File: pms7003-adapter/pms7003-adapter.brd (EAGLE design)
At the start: 36.7 x 19.8 mm, 8 parts, among them J1 LPPB052CFFN-RC, U1 ATECC508A-SSHDA-T

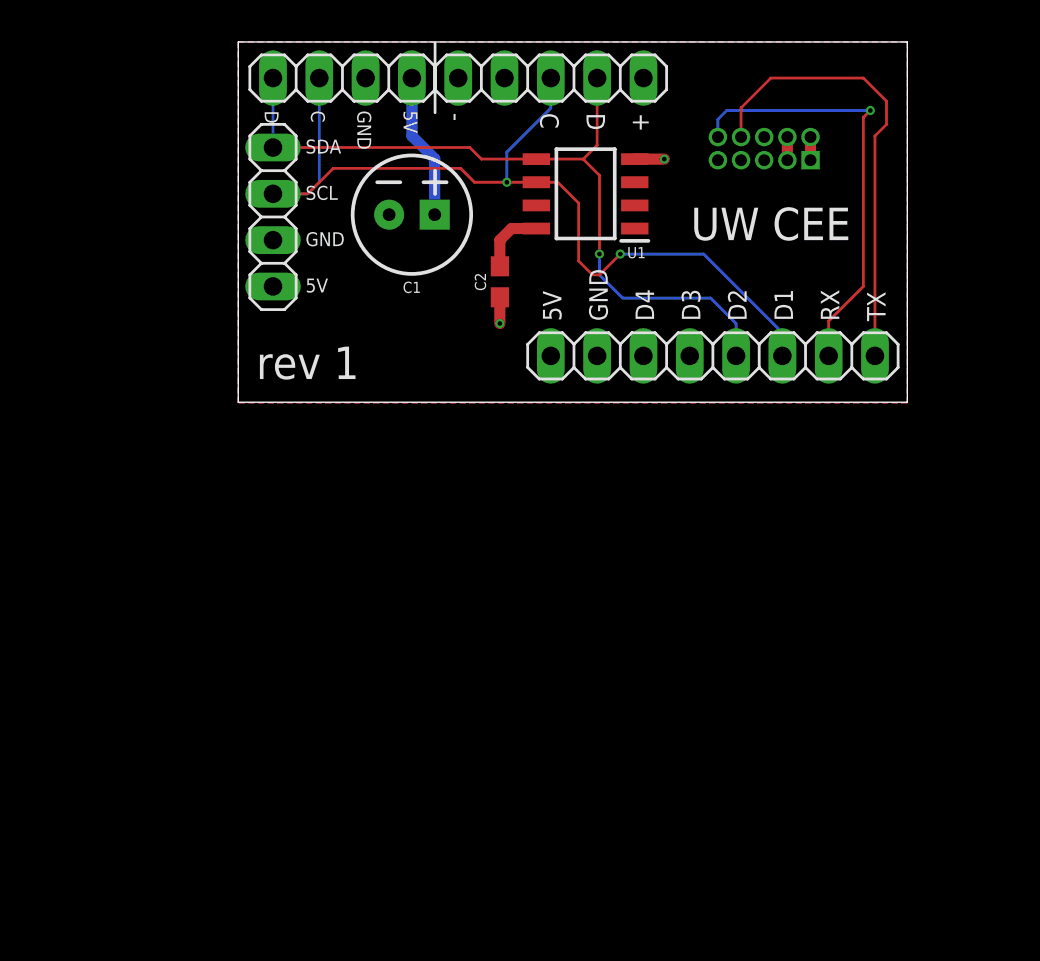
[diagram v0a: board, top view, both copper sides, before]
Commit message: Refactored for CO2 sensor and different UART pins
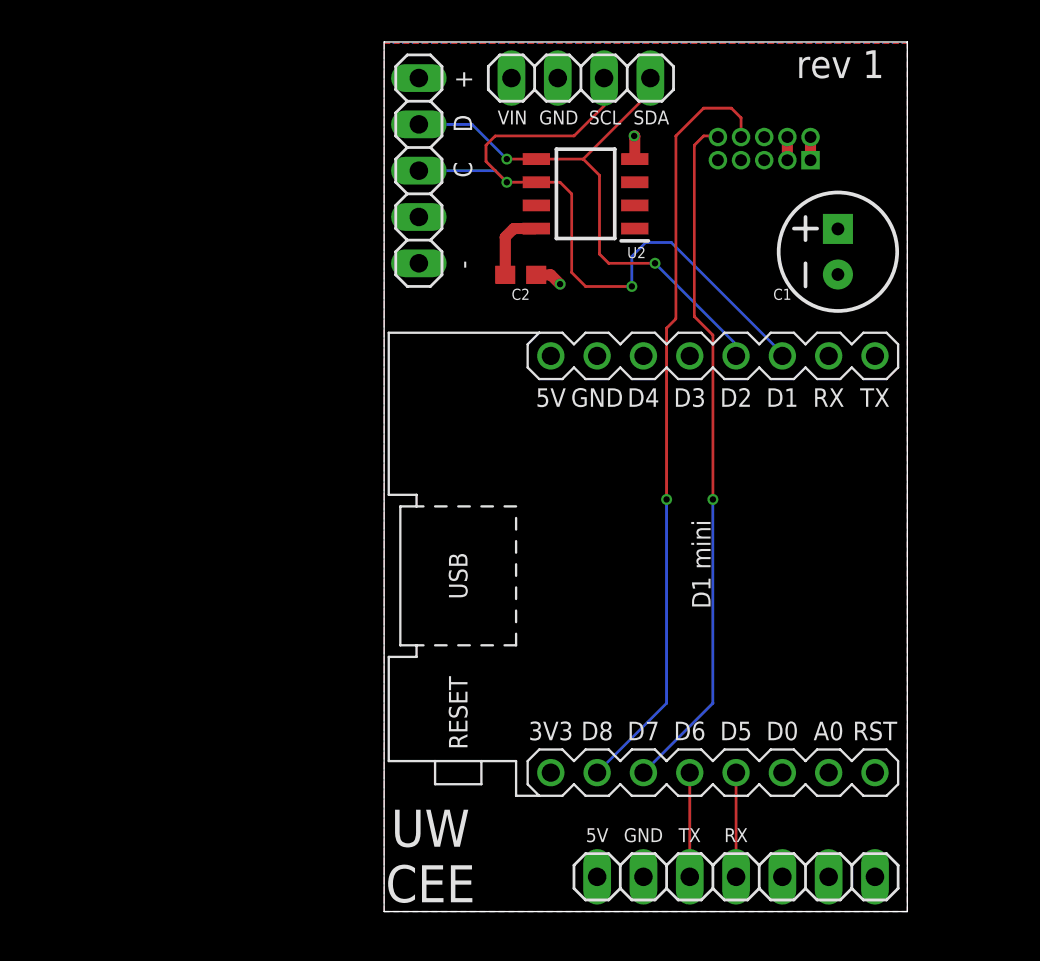
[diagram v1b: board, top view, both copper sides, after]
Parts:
- removed J5: (no value), pinhead:1X04
- added U2: ATECC508A-SSHDA-T, aqm-parts:SOIC127P600X175-8N
- J4: device pinhead:1X08 -> pinhead:1X07
- U1: value ATECC508A-SSHDA-T -> WEMOS-D1-MINI; device aqm-parts:SOIC127P600X175-8N -> aqm-parts:WEMOS-D1-MINI
- moved J4 28.6 mm to (27.3, 1.91), turned to 0 degrees
- moved C1 23.5 mm to (32.9, 36.2), turned to 90 degrees
- moved U1 21.3 mm to (25.4, 19.1), turned to 270 degrees
- moved J2 18.5 mm to (18.8, 45.7), turned to 180 degrees
- moved J3 8.84 mm to (9.91, 40.6), turned to 270 degrees
- moved C2 1.20 mm to (15.5, 34.9), turned to 0 degrees
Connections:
- new net 3V3: U1.JP1.8
- new net CO2_RX: J4.4, U1.JP1.4
- new net CO2_TX: J4.3, U1.JP1.5
- net 5V: now also J4.1, U1.JP2.8, U2.8; no longer J4.8, J5.4, U1.8
- net GND: now also J4.2, U1.JP2.7, U2.4; no longer J4.7, J5.3, U1.4
- net PM_RX: now also U1.JP1.7; no longer J4.1
- net PM_TX: now also U1.JP1.6; no longer J4.2
- net SCL: now also U1.JP2.3, U2.6; no longer J4.3, J5.2, U1.6
- net SDA: now also U1.JP2.4, U2.5; no longer J4.4, J5.1, U1.5
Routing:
- net PM_RX: track 25.0 -> 42.2 mm, vias 0 -> 1
- net PM_TX: track 23.9 -> 37.9 mm
- net SDA: track 42.9 -> 31.5 mm, vias 1 -> 2
- net SCL: track 51.6 -> 41.1 mm
- net 5V: track 13.0 -> 5.24 mm
- net CO2_TX: track 0.00 -> 5.71 mm
- net CO2_RX: track 0.00 -> 5.71 mm
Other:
- board size 36.7 x 19.8 mm -> 28.7 x 47.7 mm
- board text added: "BME"
- board text added: "CO2"
- board text added: "PMS"
- board text added: "RTC"
- board text added: "VIN"
- board text removed: "D1"
- board text removed: "D2"
- board text removed: "D3"
- board text removed: "D4"

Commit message: Resized CO2 sensor connector, ripped up all traces for redesign
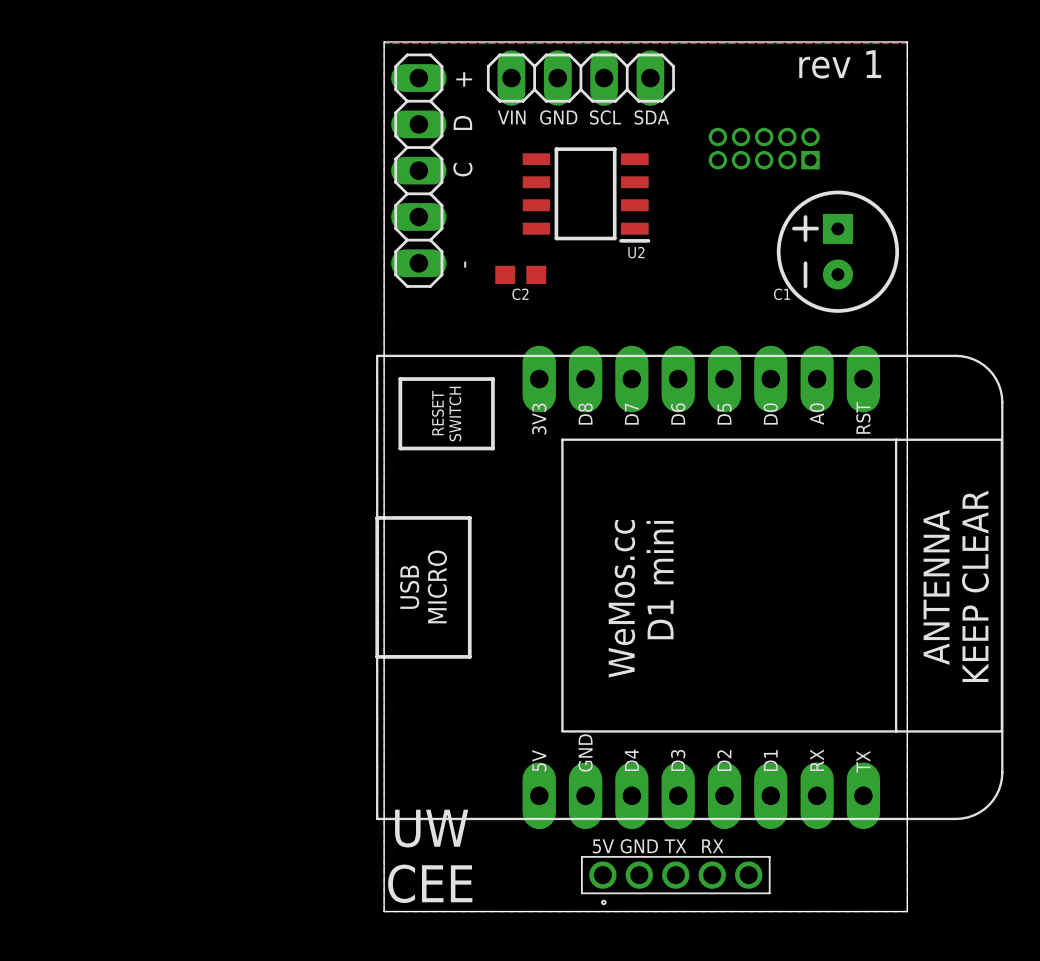
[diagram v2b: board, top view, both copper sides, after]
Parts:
- J4: value (none) -> SQT-105-01-F-S; device pinhead:1X07 -> aqm-parts:SQT-105-01-XX-S
- U1: value WEMOS-D1-MINI -> (none)
- moved J4 7.31 mm to (20.0, 2.00)
- moved U1 1.27 mm to (26.7, 19.1)
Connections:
- removed net 3V3: U1.JP1.8
- net 5V: now also U1.5V; no longer U1.JP2.8
- net CO2_RX: now also U1.D5; no longer U1.JP1.4
- net CO2_TX: now also U1.D6; no longer U1.JP1.5
- net GND: now also U1.GND; no longer U1.JP2.7
- net PM_RX: now also U1.D8; no longer U1.JP1.7
- net PM_TX: now also U1.D7; no longer U1.JP1.6
- net SCL: now also U1.D1; no longer U1.JP2.3
- net SDA: now also U1.D2; no longer U1.JP2.4
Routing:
- net PM_RX: track 42.2 -> 0.00 mm, vias 1 -> 0
- net SCL: track 41.1 -> 0.00 mm, vias 2 -> 0
- net PM_TX: track 37.9 -> 0.00 mm, vias 1 -> 0
- net SDA: track 31.5 -> 0.00 mm, vias 2 -> 0
- net CO2_TX: track 5.71 -> 0.00 mm
- net CO2_RX: track 5.71 -> 0.00 mm
- net 5V: track 5.24 -> 0.00 mm
- net GND: track 4.09 -> 0.00 mm, vias 2 -> 0

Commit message: Added an improved D1 mini footprint
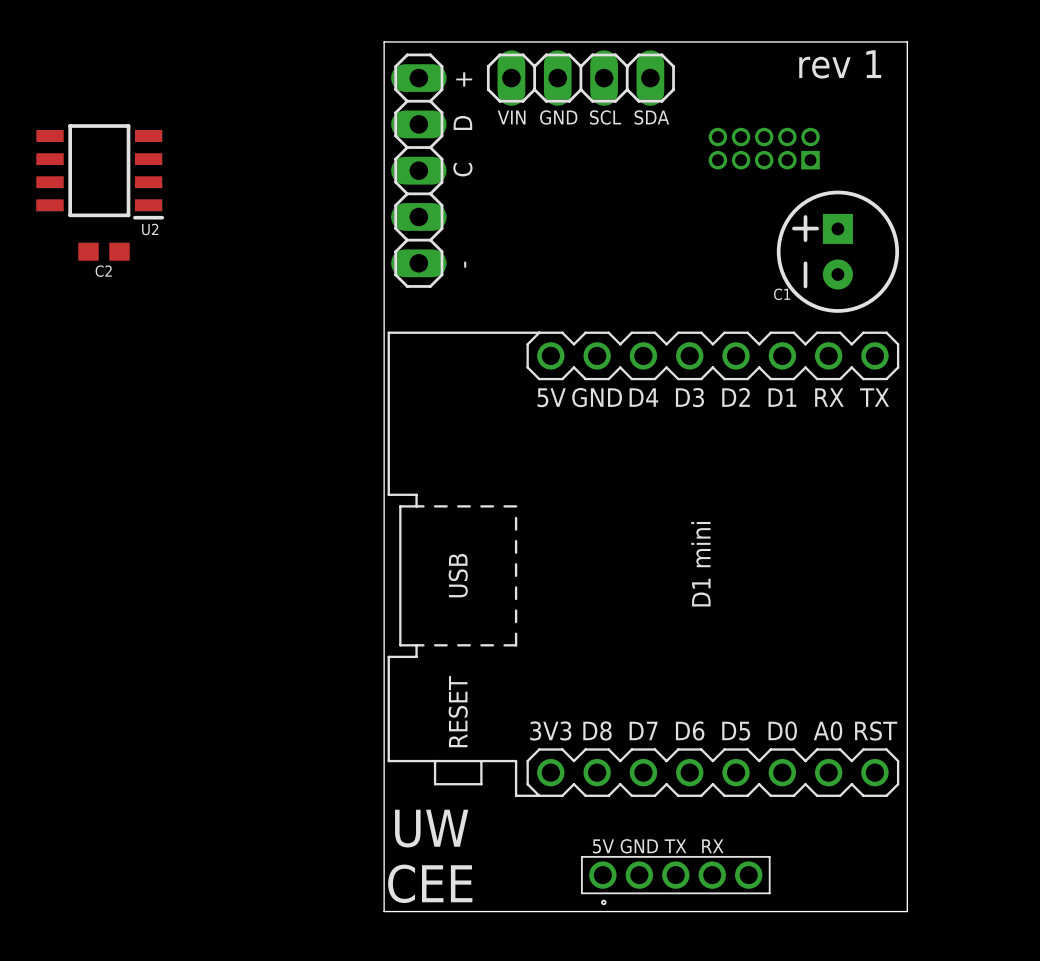
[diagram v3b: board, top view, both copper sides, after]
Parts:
- moved U2 26.7 mm to (-7.62, 40.6)
- moved C2 22.9 mm to (-7.37, 36.2)
- moved U1 1.27 mm to (25.4, 19.1)
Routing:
- removed copper zone on layer 1, net 5V
- removed copper zone on layer 16, net GND

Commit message: rev 2 board ready for fab!
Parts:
- added J5: (no value), pinhead:1X05
- J4: value SQT-105-01-F-S -> SQT-107-01-F-S; device aqm-parts:SQT-105-01-XX-S -> aqm-parts:SQT-107-01-XX-S
- moved U2 44.9 mm to (33.0, 21.6), turned to 90 degrees
- moved C2 38.8 mm to (28.6, 21.6), turned to 270 degrees
- moved C1 16.8 mm to (16.1, 36.1), turned to 180 degrees
- moved J4 12.0 mm to (32.0, 2.00), turned to 180 degrees
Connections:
- net 5V: now also J5.1
- net CO2_RX: now also U1.D0; no longer U1.D5
- net CO2_TX: now also U1.D5; no longer U1.D6
- net GND: now also J5.2
- net PM_RX: now also U1.D7; no longer U1.D8
- net PM_TX: now also U1.D6; no longer U1.D7
- net SCL: now also J5.3
- net SDA: now also J5.4
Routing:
- net SDA: track 0.00 -> 57.3 mm, vias 0 -> 2
- net SCL: track 0.00 -> 49.9 mm, vias 0 -> 6
- net PM_RX: track 0.00 -> 42.3 mm, vias 0 -> 2
- net PM_TX: track 0.00 -> 37.2 mm, vias 0 -> 2
- net GND: track 0.00 -> 16.9 mm, vias 0 -> 2
- net 5V: track 0.00 -> 10.3 mm
- net CO2_RX: track 0.00 -> 7.21 mm
- net CO2_TX: track 0.00 -> 5.91 mm
- added copper zone on layer 1, net 5V
- added copper zone on layer 16, net GND
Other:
- board text added: "LUX"
- board text added: "rev 2"
- board text removed: "rev 1"
